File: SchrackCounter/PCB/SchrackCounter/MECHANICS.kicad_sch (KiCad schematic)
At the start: 26 parts, among them J2 MEM2067-02-180-00, SW2 SW_Push, SW3 SW_Push, SW4 SW_Push, SW5 SW_Push, SW6 SW_Push, U8 74HC14

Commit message: SchrackMulticlock update
Schematic and PCB update
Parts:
- renumbered C10 to C11, C11 to C12, C12 to C13, C13 to C14, C14 to C15, C15 to C16, C16 to C17, R12 to R13, R13 to R14, R14 to R15, R15 to R16, R16 to R17, R17 to R18, R18 to R19, R19 to R20

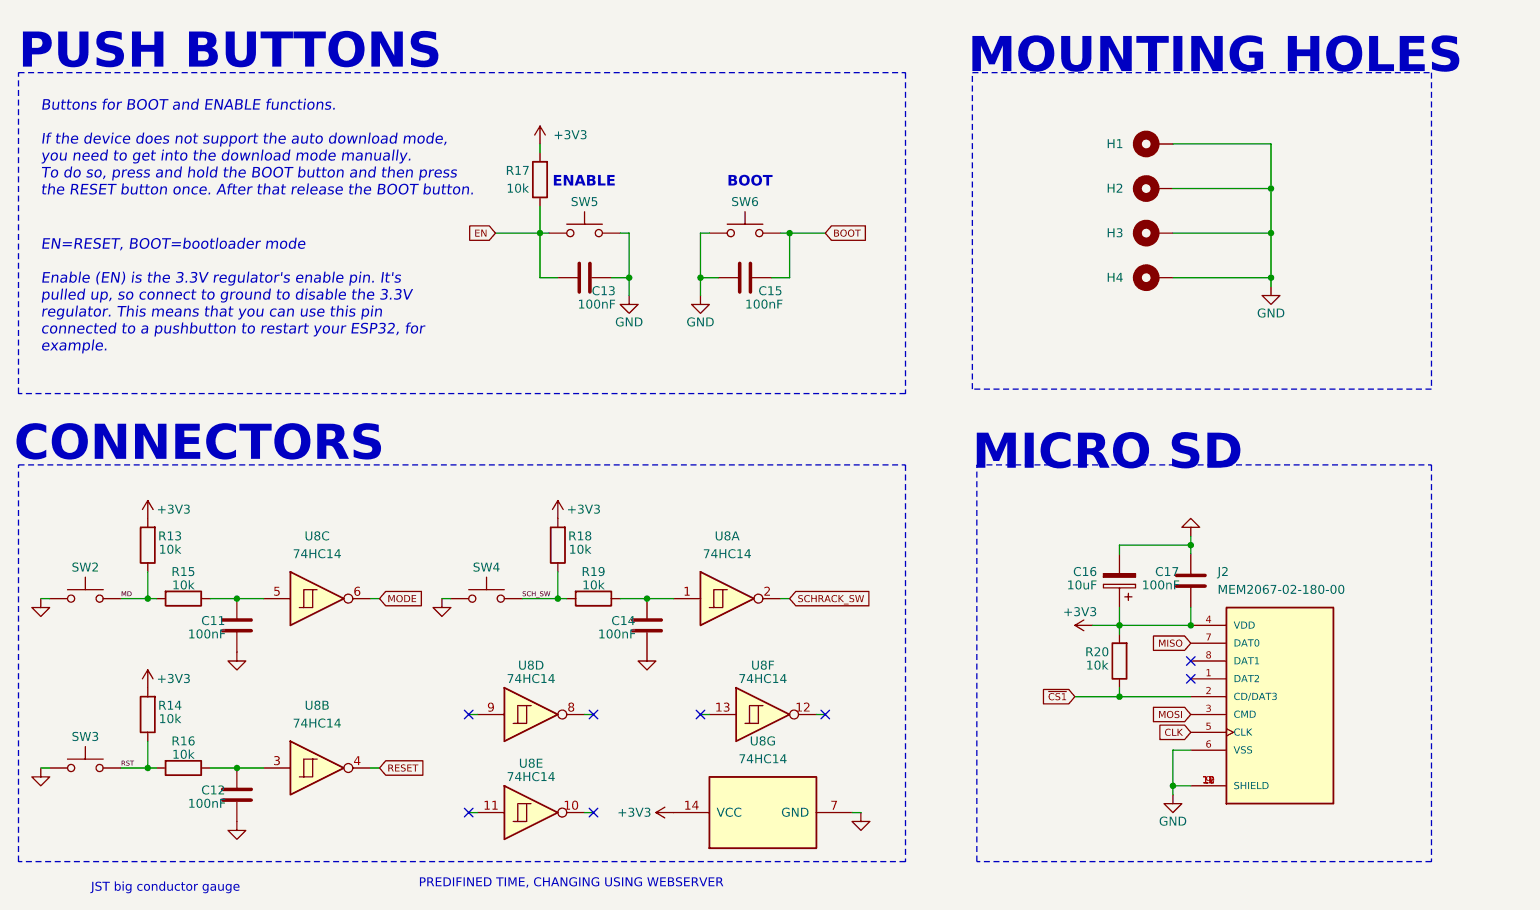
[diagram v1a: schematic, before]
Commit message: SchrackMulticlock and Counter pcb updates
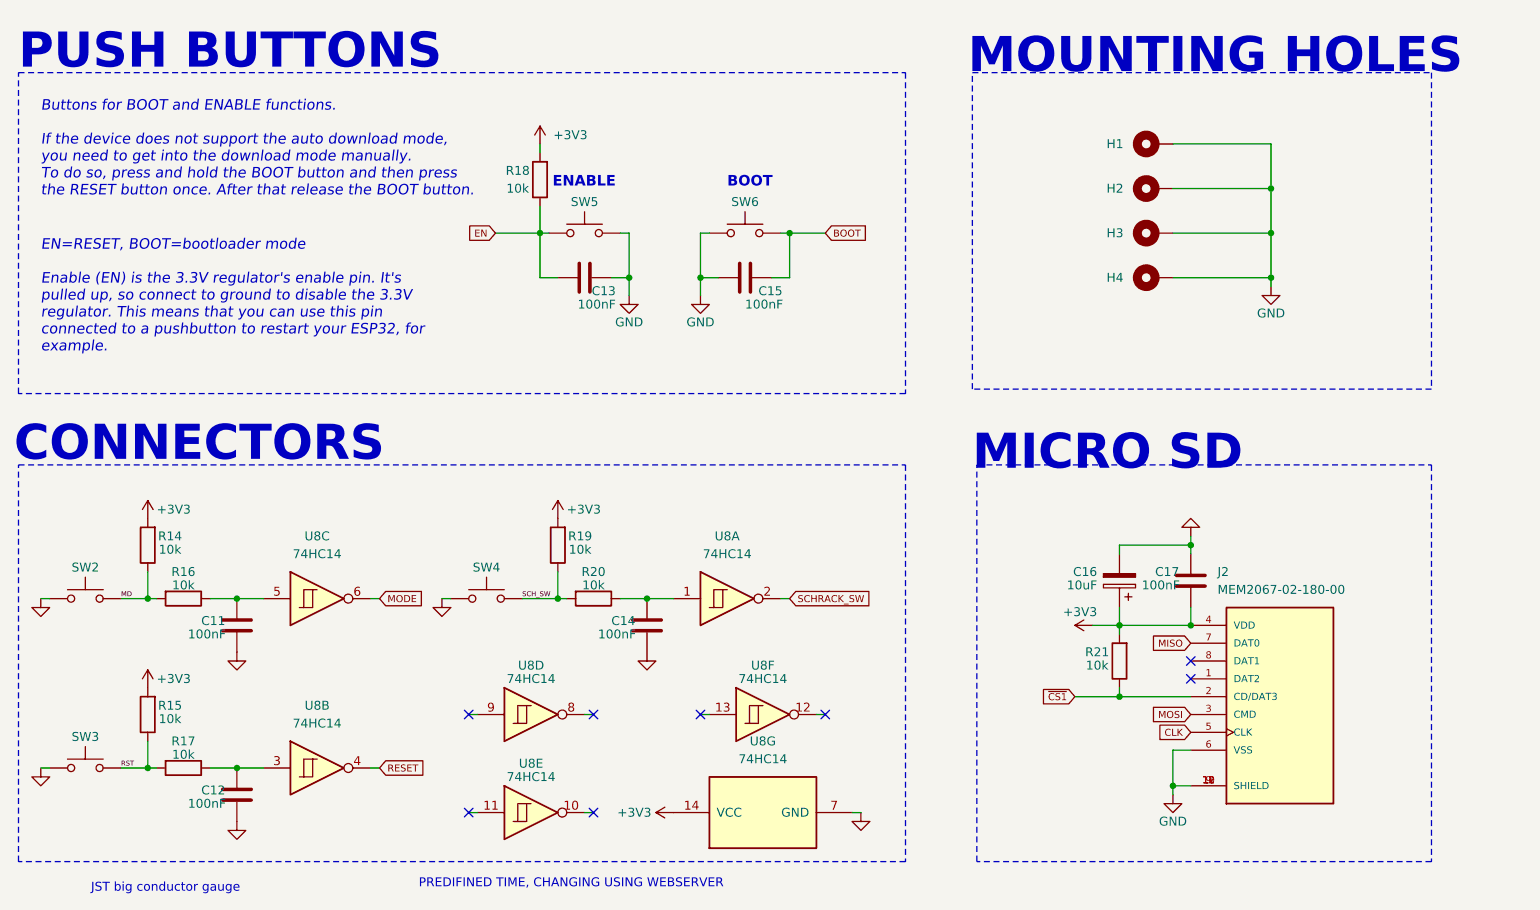
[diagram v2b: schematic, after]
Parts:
- renumbered R13 to R14, R14 to R15, R15 to R16, R16 to R17, R17 to R18, R18 to R19, R19 to R20, R20 to R21
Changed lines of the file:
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@@
 		(on_board yes)
 		(dnp no)
-		(property "Reference" "#PWR033"
+		(property "Reference" "#PWR035"
 			(at 114.3 39.37 0)
 			(effects
@@
 			(project "SchrackCounter"
 				(path "/d96f2ffc-3f4c-4f71-b693-29f6b8c3245d/0ccd8f36-c6f2-454f-91e2-c1976b699e0e"
-					(reference "#PWR033")
+					(reference "#PWR035")
 					(unit 1)
 				)
@@
 		(on_board yes)
 		(dnp no)
-		(property "Reference" "#PWR030"
+		(property "Reference" "#PWR032"
 			(at 71.12 114.3 0)
 			(effects
@@
 			(project "SchrackCounter"
 				(path "/d96f2ffc-3f4c-4f71-b693-29f6b8c3245d/0ccd8f36-c6f2-454f-91e2-c1976b699e0e"
-					(reference "#PWR030")
+					(reference "#PWR032")
 					(unit 1)
 				)
@@
 		(on_board yes)
 		(dnp no)
-		(property "Reference" "R16"
+		(property "Reference" "R17"
 			(at 63.5 120.65 90)
 			(effects
@@
 			(project "SchrackCounter"
 				(path "/d96f2ffc-3f4c-4f71-b693-29f6b8c3245d/0ccd8f36-c6f2-454f-91e2-c1976b699e0e"
-					(reference "R16")
+					(reference "R17")
 					(unit 1)
 				)
@@
 		(on_board yes)
 		(dnp no)
-		(property "Reference" "#PWR041"
+		(property "Reference" "#PWR043"
 			(at 204.47 134.62 0)
 			(effects
@@
 			(project "SchrackCounter"
 				(path "/d96f2ffc-3f4c-4f71-b693-29f6b8c3245d/0ccd8f36-c6f2-454f-91e2-c1976b699e0e"
-					(reference "#PWR041")
+					(reference "#PWR043")
 					(unit 1)
 				)
@@
 		(on_board yes)
 		(dnp no)
-		(property "Reference" "#PWR040"
+		(property "Reference" "#PWR042"
 			(at 196.85 104.14 0)
 			(effects
@@
 			(project "SchrackCounter"
 				(path "/d96f2ffc-3f4c-4f71-b693-29f6b8c3245d/0ccd8f36-c6f2-454f-91e2-c1976b699e0e"
-					(reference "#PWR040")
+					(reference "#PWR042")
 					(unit 1)
 				)
@@
 		(on_board yes)
 		(dnp no)
-		(property "Reference" "#PWR038"
+		(property "Reference" "#PWR040"
 			(at 137.16 63.5 0)
 			(effects
@@
 			(project "SchrackCounter"
 				(path "/d96f2ffc-3f4c-4f71-b693-29f6b8c3245d/0ccd8f36-c6f2-454f-91e2-c1976b699e0e"
-					(reference "#PWR038")
+					(reference "#PWR040")
 					(unit 1)
 				)
@@
 		(on_board yes)
 		(dnp no)
-		(property "Reference" "#PWR035"
+		(property "Reference" "#PWR037"
 			(at 127 63.5 0)
 			(effects
@@
 			(project "SchrackCounter"
 				(path "/d96f2ffc-3f4c-4f71-b693-29f6b8c3245d/0ccd8f36-c6f2-454f-91e2-c1976b699e0e"
-					(reference "#PWR035")
+					(reference "#PWR037")
 					(unit 1)
 				)
@@
 		(on_board yes)
 		(dnp no)
-		(property "Reference" "#PWR026"
+		(property "Reference" "#PWR028"
 			(at 43.18 106.68 0)
 			(effects
@@
 			(project "SchrackCounter"
 				(path "/d96f2ffc-3f4c-4f71-b693-29f6b8c3245d/0ccd8f36-c6f2-454f-91e2-c1976b699e0e"
-					(reference "#PWR026")
+					(reference "#PWR028")
 					(unit 1)
 				)
@@
 		(on_board yes)
 		(dnp no)
-		(property "Reference" "#PWR028"
+		(property "Reference" "#PWR030"
 			(at 58.42 92.71 0)
 			(effects
@@
 			(project "SchrackCounter"
 				(path "/d96f2ffc-3f4c-4f71-b693-29f6b8c3245d/0ccd8f36-c6f2-454f-91e2-c1976b699e0e"
-					(reference "#PWR028")
+					(reference "#PWR030")
 					(unit 1)
 				)
@@
 		(on_board yes)
 		(dnp no)
-		(property "Reference" "#PWR032"
+		(property "Reference" "#PWR034"
 			(at 100.33 106.68 0)
 			(effects
@@
 			(project "SchrackCounter"
 				(path "/d96f2ffc-3f4c-4f71-b693-29f6b8c3245d/0ccd8f36-c6f2-454f-91e2-c1976b699e0e"
-					(reference "#PWR032")
+					(reference "#PWR034")
 					(unit 1)
 				)
@@
 		(on_board yes)
 		(dnp no)
-		(property "Reference" "R17"
+		(property "Reference" "R18"
 			(at 111.125 39.37 0)
 			(effects
@@
 			(project "SchrackCounter"
 				(path "/d96f2ffc-3f4c-4f71-b693-29f6b8c3245d/0ccd8f36-c6f2-454f-91e2-c1976b699e0e"
-					(reference "R17")
+					(reference "R18")
 					(unit 1)
 				)
@@
 		(on_board yes)
 		(dnp no)
-		(property "Reference" "#PWR042"
+		(property "Reference" "#PWR044"
 			(at 207.01 85.09 0)
 			(effects
@@
 			(project "SchrackCounter"
 				(path "/d96f2ffc-3f4c-4f71-b693-29f6b8c3245d/0ccd8f36-c6f2-454f-91e2-c1976b699e0e"
-					(reference "#PWR042")
+					(reference "#PWR044")
 					(unit 1)
 				)
@@
 		(on_board yes)
 		(dnp no)
-		(property "Reference" "R14"
+		(property "Reference" "R15"
 			(at 61.595 115.57 0)
 			(effects
@@
 			(project "SchrackCounter"
 				(path "/d96f2ffc-3f4c-4f71-b693-29f6b8c3245d/0ccd8f36-c6f2-454f-91e2-c1976b699e0e"
-					(reference "R14")
+					(reference "R15")
 					(unit 1)
 				)
@@
 		(on_board yes)
 		(dnp no)
-		(property "Reference" "#PWR043"
+		(property "Reference" "#PWR045"
 			(at 218.44 62.23 0)
 			(effects
@@
 			(project "SchrackCounter"
 				(path "/d96f2ffc-3f4c-4f71-b693-29f6b8c3245d/0ccd8f36-c6f2-454f-91e2-c1976b699e0e"
-					(reference "#PWR043")
+					(reference "#PWR045")
 					(unit 1)
 				)
@@
 		(on_board yes)
 		(dnp no)
-		(property "Reference" "R15"
+		(property "Reference" "R16"
 			(at 63.5 96.52 90)
 			(effects
@@
 			(project "SchrackCounter"
 				(path "/d96f2ffc-3f4c-4f71-b693-29f6b8c3245d/0ccd8f36-c6f2-454f-91e2-c1976b699e0e"
-					(reference "R15")
+					(reference "R16")
 					(unit 1)
 				)
@@
 		(on_board yes)
 		(dnp no)
-		(property "Reference" "R18"
+		(property "Reference" "R19"
 			(at 120.015 91.44 0)
 			(effects
@@
 			(project "SchrackCounter"
 				(path "/d96f2ffc-3f4c-4f71-b693-29f6b8c3245d/0ccd8f36-c6f2-454f-91e2-c1976b699e0e"
-					(reference "R18")
+					(reference "R19")
 					(unit 1)
 				)
@@
 		(on_board yes)
 		(dnp no)
-		(property "Reference" "R19"
+		(property "Reference" "R20"
 			(at 121.92 96.52 90)
 			(effects
@@
 			(project "SchrackCounter"
 				(path "/d96f2ffc-3f4c-4f71-b693-29f6b8c3245d/0ccd8f36-c6f2-454f-91e2-c1976b699e0e"
-					(reference "R19")
+					(reference "R20")
 					(unit 1)
 				)
@@
 		(on_board yes)
 		(dnp no)
-		(property "Reference" "#PWR029"
+		(property "Reference" "#PWR031"
 			(at 58.42 116.84 0)
 			(effects
@@
 			(project "SchrackCounter"
 				(path "/d96f2ffc-3f4c-4f71-b693-29f6b8c3245d/0ccd8f36-c6f2-454f-91e2-c1976b699e0e"
-					(reference "#PWR029")
+					(reference "#PWR031")
 					(unit 1)
 				)
@@
 		(on_board yes)
 		(dnp no)
-		(property "Reference" "#PWR039"
+		(property "Reference" "#PWR041"
 			(at 160.02 137.16 0)
 			(effects
@@
 			(project "SchrackCounter"
 				(path "/d96f2ffc-3f4c-4f71-b693-29f6b8c3245d/0ccd8f36-c6f2-454f-91e2-c1976b699e0e"
-					(reference "#PWR039")
+					(reference "#PWR041")
 					(unit 1)
 				)
@@
 		(on_board yes)
 		(dnp no)
-		(property "Reference" "R13"
+		(property "Reference" "R14"
 			(at 61.595 91.44 0)
 			(effects
@@
 			(project "SchrackCounter"
 				(path "/d96f2ffc-3f4c-4f71-b693-29f6b8c3245d/0ccd8f36-c6f2-454f-91e2-c1976b699e0e"
-					(reference "R13")
+					(reference "R14")
 					(unit 1)
 				)
@@
 		(on_board yes)
 		(dnp no)
-		(property "Reference" "R20"
+		(property "Reference" "R21"
 			(at 193.675 107.95 0)
 			(effects
@@
 			(project "SchrackCounter"
 				(path "/d96f2ffc-3f4c-4f71-b693-29f6b8c3245d/0ccd8f36-c6f2-454f-91e2-c1976b699e0e"
-					(reference "R20")
+					(reference "R21")
 					(unit 1)
 				)
@@
 		(on_board yes)
 		(dnp no)
-		(property "Reference" "#PWR037"
+		(property "Reference" "#PWR039"
 			(at 137.16 130.81 0)
 			(effects
@@
 			(project "SchrackCounter"
 				(path "/d96f2ffc-3f4c-4f71-b693-29f6b8c3245d/0ccd8f36-c6f2-454f-91e2-c1976b699e0e"
-					(reference "#PWR037")
+					(reference "#PWR039")
 					(unit 1)
 				)
@@
 		(on_board yes)
 		(dnp no)
-		(property "Reference" "#PWR027"
+		(property "Reference" "#PWR029"
 			(at 43.18 130.81 0)
 			(effects
@@
 			(project "SchrackCounter"
 				(path "/d96f2ffc-3f4c-4f71-b693-29f6b8c3245d/0ccd8f36-c6f2-454f-91e2-c1976b699e0e"
-					(reference "#PWR027")
+					(reference "#PWR029")
 					(unit 1)
 				)
@@
 		(on_board yes)
 		(dnp no)
-		(property "Reference" "#PWR031"
+		(property "Reference" "#PWR033"
 			(at 71.12 138.43 0)
 			(effects
@@
 			(project "SchrackCounter"
 				(path "/d96f2ffc-3f4c-4f71-b693-29f6b8c3245d/0ccd8f36-c6f2-454f-91e2-c1976b699e0e"
-					(reference "#PWR031")
+					(reference "#PWR033")
 					(unit 1)
 				)
@@
 		(on_board yes)
 		(dnp no)
-		(property "Reference" "#PWR036"
+		(property "Reference" "#PWR038"
 			(at 129.54 114.3 0)
 			(effects
@@
 			(project "SchrackCounter"
 				(path "/d96f2ffc-3f4c-4f71-b693-29f6b8c3245d/0ccd8f36-c6f2-454f-91e2-c1976b699e0e"
-					(reference "#PWR036")
+					(reference "#PWR038")
 					(unit 1)
 				)
@@
 		(on_board yes)
 		(dnp no)
-		(property "Reference" "#PWR034"
+		(property "Reference" "#PWR036"
 			(at 116.84 92.71 0)
 			(effects
@@
 			(project "SchrackCounter"
 				(path "/d96f2ffc-3f4c-4f71-b693-29f6b8c3245d/0ccd8f36-c6f2-454f-91e2-c1976b699e0e"
-					(reference "#PWR034")
+					(reference "#PWR036")
 					(unit 1)
 				)
